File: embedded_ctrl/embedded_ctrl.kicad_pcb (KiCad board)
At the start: 2 copper layers, 67.8 x 54.5 mm, 47 parts, among them J1 Conn_02x13_Odd_Even, J2 RJ11, J6 Screw_Terminal_01x02, J7 USB_B, Q1 SS8050, Q2 SS8050, U1 ESP32-WROOM-32, U2 CP2102N-A02-GQFN28, U3 R-78E3.3-1.0

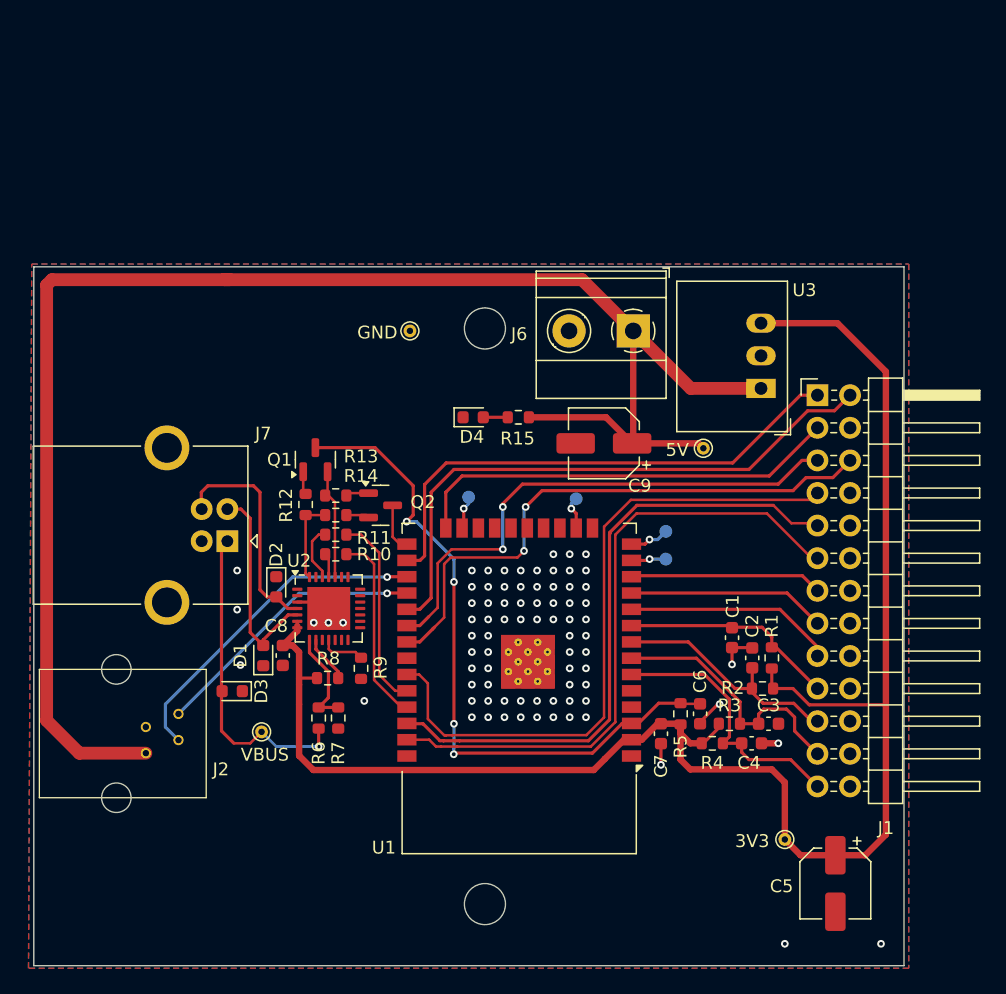
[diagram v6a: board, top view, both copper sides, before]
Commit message: Expose D36 and D39. Add buttons for EN and IO0,bodge wire passthrus, and version text
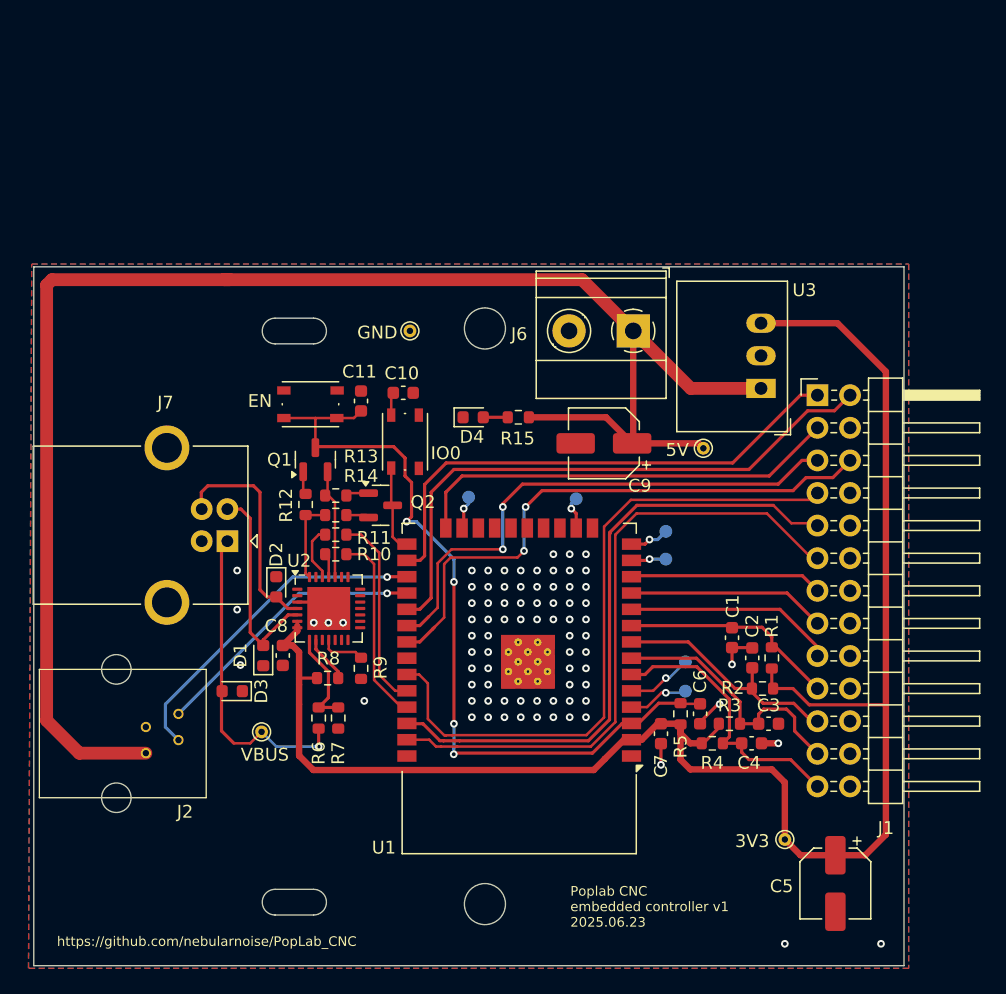
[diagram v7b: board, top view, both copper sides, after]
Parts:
- added C10: 100nF, Capacitor_SMD:C_0603_1608Metric, F.Cu at (111.0, 59.8)
- added C11: 100nF, Capacitor_SMD:C_0603_1608Metric, F.Cu at (107.7, 60.5)
- added SW1: IO0, Button_Switch_SMD:SW_Push_1P1T_NO_Vertical_Wuerth_434133025816, F.Cu at (111.1, 63.6)
- added SW2: EN, Button_Switch_SMD:SW_Push_1P1T_NO_Vertical_Wuerth_434133025816, F.Cu at (103.8, 60.7)
- added TP10: D39, TestPoint:TestPoint_Pad_D1.0mm, B.Cu at (133.0, 80.8)
- added TP9: D36, TestPoint:TestPoint_Pad_D1.0mm, B.Cu at (133.0, 83.1)
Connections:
- net EN renamed /EN
- U1 pad 4: unconnected-(U1-SENSOR_VP-Pad4) -> D36
- U1 pad 5: unconnected-(U1-SENSOR_VN-Pad5) -> D39
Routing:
- net /EN: track 52.8 -> 62.2 mm
- net D39: track 0.00 -> 5.14 mm, vias 0 -> 1
- net /IO0: track 3.81 -> 8.56 mm
- net D36: track 0.00 -> 4.71 mm, vias 0 -> 1
- net D34: track 21.2 -> 21.7 mm
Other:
- outline, holes or cut-outs redrawn
- board text added: "Poplab CNC embedded controller v1 2025.06.23"
- board text added: "https://github.com/nebularnoise/PopLab_CNC"

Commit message: add tvs diodes to uart connector
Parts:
- added D5: D_TVS, Diode_SMD:D_0603_1608Metric, F.Cu at (97.8, 84.3)
- added D6: D_TVS, Diode_SMD:D_0603_1608Metric, F.Cu at (98.0, 88.1)
- moved D3 3.16 mm to (100.8, 82.8)
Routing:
- net /IO0: track 8.56 -> 14.5 mm, vias 0 -> 2
- net /U2RXD: track 26.1 -> 30.4 mm
- net /U2TXD: track 21.7 -> 25.4 mm
- net /VBUS: track 25.2 -> 23.2 mm
- net GND: vias 80 -> 82
